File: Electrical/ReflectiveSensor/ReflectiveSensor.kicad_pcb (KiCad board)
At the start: 2 copper layers, 20.1 x 6.3 mm, 5 parts, among them J1 Refl_Mount, K1 QRE1113GR

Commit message: Finalize Reflective Opto Sensor
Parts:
- added C1: 0.1 uF, Capacitor_SMD:C_0805_2012Metric_Pad1.18x1.45mm_HandSolder, B.Cu at (351.8, 200.2)
- moved J1 185.1 mm to (354.7, 197.8)
- moved K1 185.1 mm to (348.2, 199.1)
- moved R1 185.1 mm to (345.7, 199.1)
- moved H1 185.1 mm to (361.8, 199.1)
- moved R2 182.8 mm to (348.9, 197.7), turned to 180 degrees
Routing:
- net Net-(J1-Pin_2): track 14.9 -> 21.8 mm
- net Net-(J1-Pin_1): track 11.1 -> 13.6 mm
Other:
- board size 20.1 x 6.3 mm -> 21.2 x 6.3 mm
- board text added: "locked"

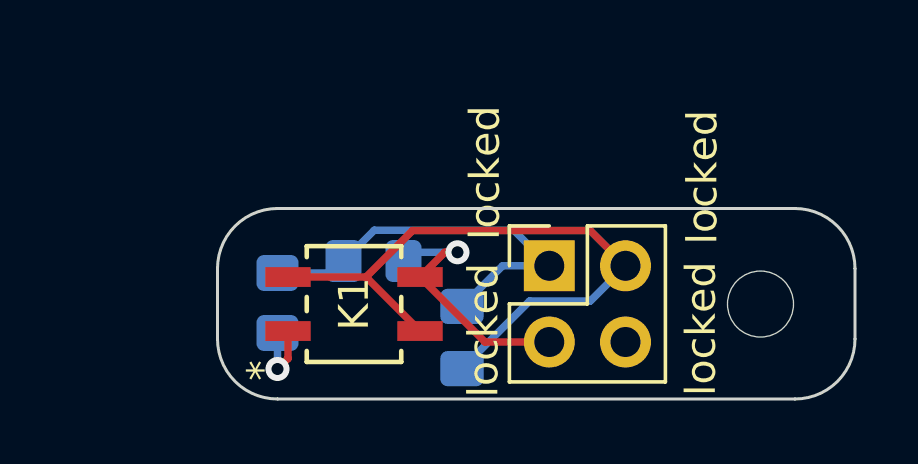
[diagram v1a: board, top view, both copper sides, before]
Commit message: Resize the reflective sensor
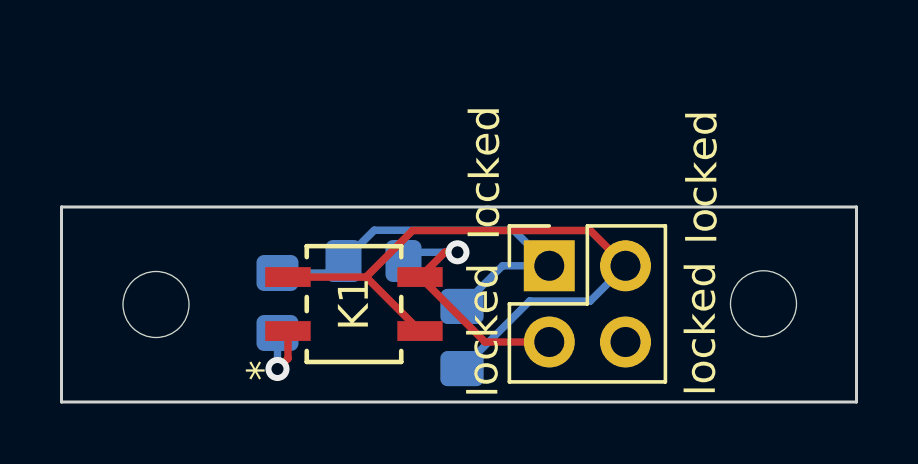
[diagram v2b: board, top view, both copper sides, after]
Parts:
- added H2: MountingHole, MountingHole:MountingHole_2.2mm_M2, F.Cu at (341.6, 199.1)
- moved H1 0.10 mm to (361.9, 199.1)
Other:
- board size 21.2 x 6.3 mm -> 26.5 x 6.5 mm
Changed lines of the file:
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@@
   (net 5 "Net-(K1-Pad1)")
   (footprint "MountingHole:MountingHole_2.2mm_M2" locked (layer "F.Cu")
-    (at 361.775 199.085)
+    (at 361.875 199.075)
     (descr "Mounting Hole 2.2mm, no annular, M2")
     (tags "mounting hole 2.2mm no annular m2")
@@
     (pad "4" smd rect locked (at 0.900001 -2.20345 90) (size 0.6604 1.5113) (layers "F.Cu" "F.Paste" "F.Mask")
       (net 2 "Net-(J1-Pin_2)") (pinfunction "4") (pintype "passive"))
+  )
+  (footprint "MountingHole:MountingHole_2.2mm_M2" locked (layer "F.Cu")
+    (at 341.625 199.1)
+    (descr "Mounting Hole 2.2mm, no annular, M2")
+    (tags "mounting hole 2.2mm no annular m2")
+    (property "Description" "")
+    (property "Mfr" "")
+    (property "Mfr P/N" "")
+    (property "Sheetfile" "ReflectiveSensor.kicad_sch")
+    (property "Sheetname" "")
+    (property "Supplier 1" "")
+    (property "Supplier 1 P/N" "")
+    (property "Supplier 2" "")
+    (property "Supplier 2 P/N" "")
+    (property "exclude_from_bom" "")
+    (property "ki_description" "Mounting Hole without connection")
+    (property "ki_keywords" "mounting hole")
+    (attr exclude_from_pos_files exclude_from_bom)
+    (fp_text reference "H2" (at 0 -3.2) (layer "F.SilkS") hide
+        (effects (font (size 1 1) (thickness 0.15)))
+    )
+    (fp_text value "MountingHole" (at 0 3.2) (layer "F.Fab") hide
+        (effects (font (size 1 1) (thickness 0.15)))
+    )
+    (fp_text user "${REFERENCE}" (at 0 0.05) (layer "F.Fab")
+        (effects (font (size 1 1) (thickness 0.15)))
+    )
+    (fp_circle (center 0 0) (end 2.2 0)
+      (stroke (width 0.15) (type solid)) (fill none) (layer "Cmts.User"))
+    (fp_circle (center 0 0) (end 2.45 0)
+      (stroke (width 0.05) (type solid)) (fill none) (layer "F.CrtYd"))
+    (pad "" np_thru_hole circle locked (at 0 0) (size 2.2 2.2) (drill 2.2) (layers "*.Cu" "*.Mask"))
   )
   (footprint "Connector_PinHeader_2.54mm:PinHeader_2x02_P2.54mm_Vertical" locked (layer "F.Cu")
@@
     )
   )
-  (gr_arc locked (start 362.925 195.9) (mid 364.339214 196.485786) (end 364.925 197.9)
-    (stroke (width 0.1) (type default)) (layer "Edge.Cuts"))
-  (gr_arc locked (start 345.675 202.25) (mid 344.260786 201.664214) (end 343.675 200.25)
-    (stroke (width 0.1) (type default)) (layer "Edge.Cuts"))
-  (gr_line locked (start 345.675 195.9) (end 362.925 195.9)
-    (stroke (width 0.1) (type default)) (layer "Edge.Cuts"))
-  (gr_line locked (start 364.925 197.9) (end 364.925 200.25)
-    (stroke (width 0.1) (type default)) (layer "Edge.Cuts"))
-  (gr_arc locked (start 343.675 197.9) (mid 344.260786 196.485786) (end 345.675 195.9)
-    (stroke (width 0.1) (type default)) (layer "Edge.Cuts"))
-  (gr_line locked (start 362.925 202.25) (end 345.675 202.25)
-    (stroke (width 0.1) (type default)) (layer "Edge.Cuts"))
-  (gr_arc locked (start 364.925 200.25) (mid 364.339214 201.664214) (end 362.925 202.25)
-    (stroke (width 0.1) (type default)) (layer "Edge.Cuts"))
-  (gr_line locked (start 343.675 200.25) (end 343.675 197.9)
-    (stroke (width 0.1) (type default)) (layer "Edge.Cuts"))
+  (gr_rect locked (start 338.475 195.85) (end 364.975 202.35)
+    (stroke (width 0.1) (type default)) (fill none) (layer "Edge.Cuts"))
   (gr_text locked "G" (at 360.425 197.1 90) (layer "F.SilkS")
     (effects (font (size 1 1) (thickness 0.15)) (justify left bottom))

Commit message: Finish final board design for Rev 0.1 Main board and reflective Sensor. Created Gerbers.
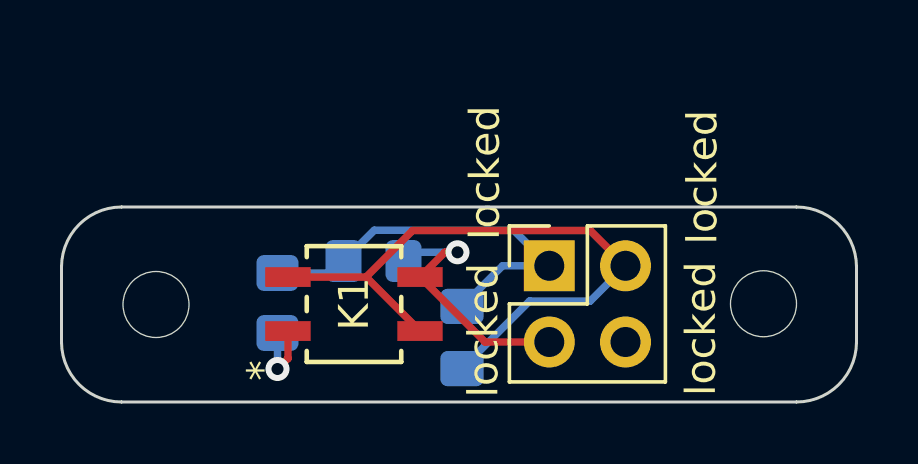
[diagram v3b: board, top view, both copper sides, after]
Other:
- outline, holes or cut-outs redrawn
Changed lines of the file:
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@@
     (fp_line (start 1 0.625) (end 1 -0.625)
       (stroke (width 0.1) (type solid)) (layer "B.Fab"))
-    (pad "1" smd roundrect locked (at -1.0375 0 270) (size 1.175 1.45) (layers "B.Cu" "B.Paste" "B.Mask") (roundrect_rratio 0.212766)
+    (pad "1" smd roundrect locked (at -1.0375 0 270) (size 1.175 1.45) (layers "B.Cu" "B.Paste" "B.Mask") (roundrect_rratio 0.2127659574)
       (net 1 "Net-(J1-Pin_1)") (pintype "passive"))
-    (pad "2" smd roundrect locked (at 1.0375 0 270) (size 1.175 1.45) (layers "B.Cu" "B.Paste" "B.Mask") (roundrect_rratio 0.212766)
+    (pad "2" smd roundrect locked (at 1.0375 0 270) (size 1.175 1.45) (layers "B.Cu" "B.Paste" "B.Mask") (roundrect_rratio 0.2127659574)
       (net 2 "Net-(J1-Pin_2)") (pintype "passive"))
     (model "${KICAD6_3DMODEL_DIR}/Capacitor_SMD.3dshapes/C_0805_2012Metric.wrl"
@@
     )
   )
-  (gr_rect locked (start 338.475 195.85) (end 364.975 202.35)
-    (stroke (width 0.1) (type default)) (fill none) (layer "Edge.Cuts"))
+  (gr_arc (start 340.475 202.35) (mid 339.060786 201.764214) (end 338.475 200.35)
+    (stroke (width 0.1) (type default)) (layer "Edge.Cuts"))
+  (gr_arc (start 338.475 197.85) (mid 339.060786 196.435786) (end 340.475 195.85)
+    (stroke (width 0.1) (type default)) (layer "Edge.Cuts"))
+  (gr_line (start 338.475 200.35) (end 338.475 197.85)
+    (stroke (width 0.1) (type default)) (layer "Edge.Cuts"))
+  (gr_line (start 364.975 197.85) (end 364.975 200.35)
+    (stroke (width 0.1) (type default)) (layer "Edge.Cuts"))
+  (gr_line (start 362.975 202.35) (end 340.475 202.35)
+    (stroke (width 0.1) (type default)) (layer "Edge.Cuts"))
+  (gr_arc (start 362.975 195.85) (mid 364.389214 196.435786) (end 364.975 197.85)
+    (stroke (width 0.1) (type default)) (layer "Edge.Cuts"))
+  (gr_line (start 340.475 195.85) (end 362.975 195.85)
+    (stroke (width 0.1) (type default)) (layer "Edge.Cuts"))
+  (gr_arc (start 364.975 200.35) (mid 364.389214 201.764214) (end 362.975 202.35)
+    (stroke (width 0.1) (type default)) (layer "Edge.Cuts"))
   (gr_text locked "G" (at 360.425 197.1 90) (layer "F.SilkS")
     (effects (font (size 1 1) (thickness 0.15)) (justify left bottom))
